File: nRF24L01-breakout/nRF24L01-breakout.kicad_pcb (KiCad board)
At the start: 2 copper layers, 28.6 x 16.4 mm, 17 parts, among them J1 Conn_01x04_Female, J2 Conn_01x04_Female, U1 NRF24L01, U2 Antenna_PCB_2.4GHz_50Ohm, U3 Balun_2450BM14A0002, Y1 Crystal_GND24_Small

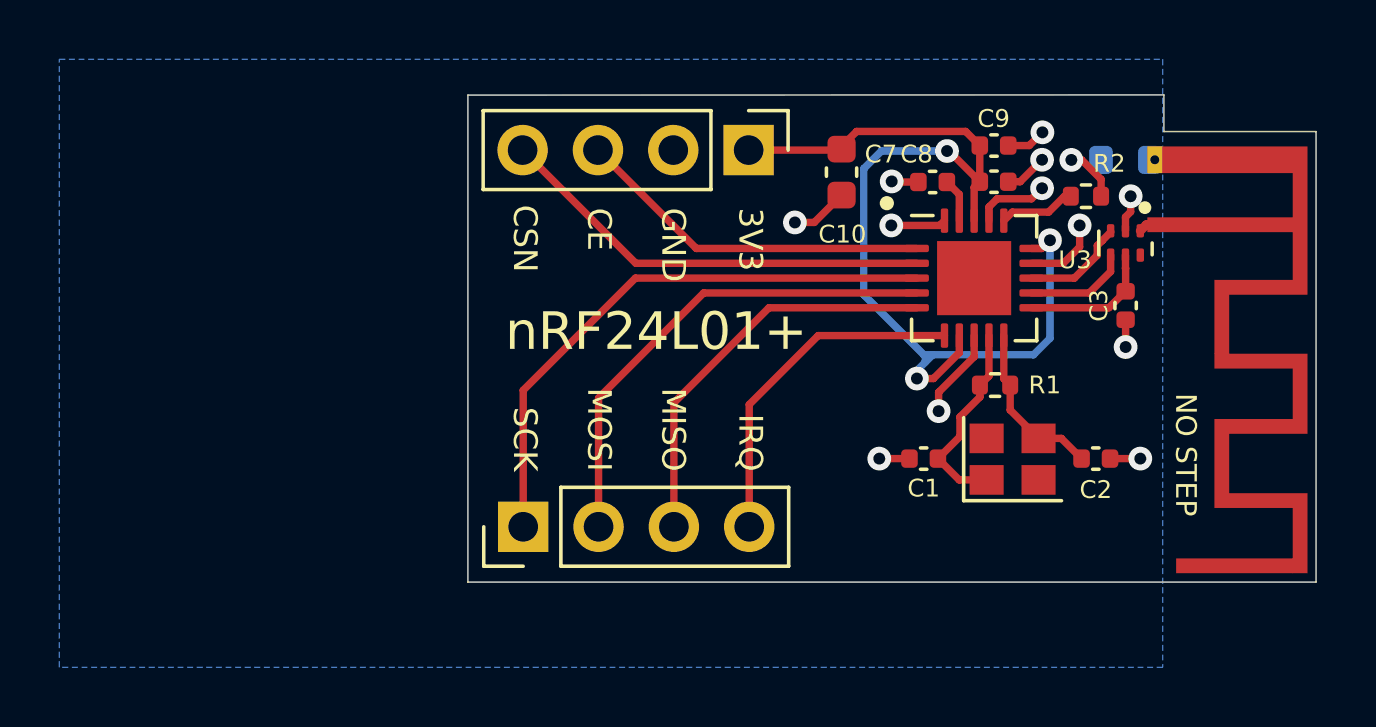
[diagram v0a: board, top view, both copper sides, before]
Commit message: Spread out signal traces
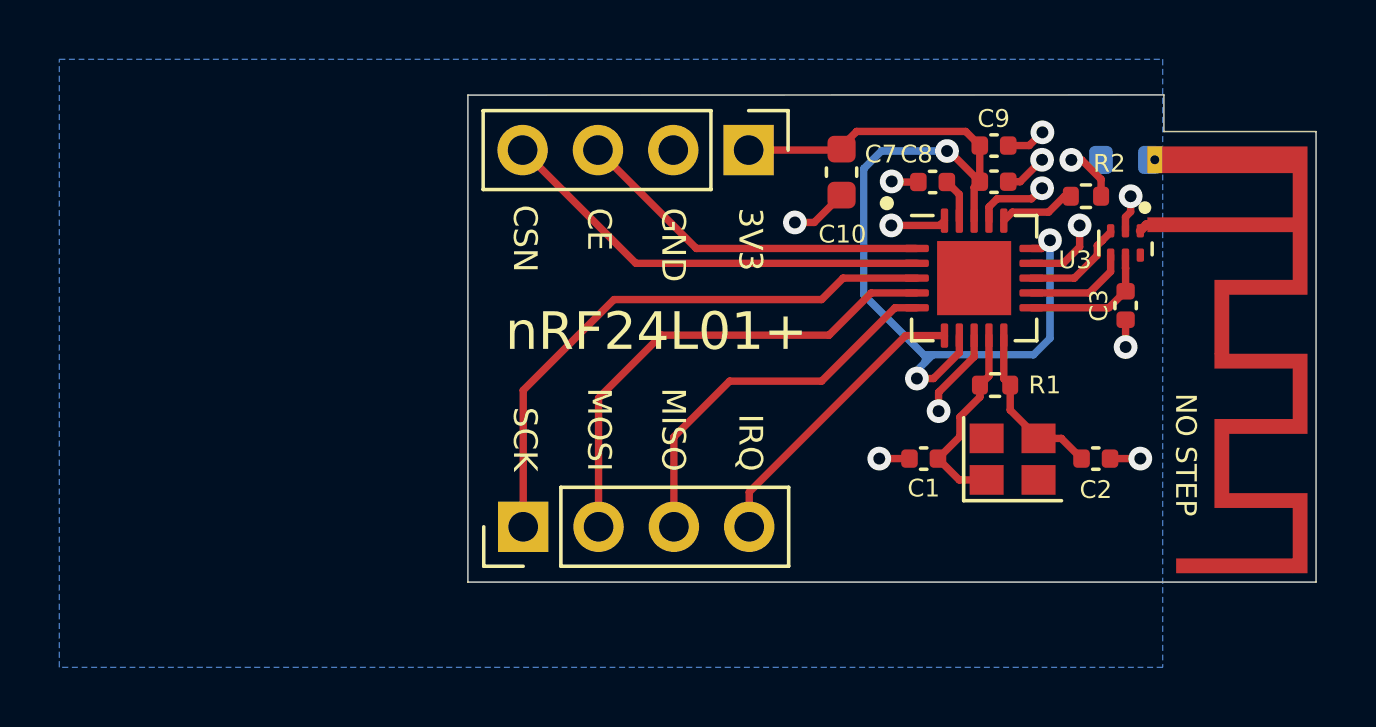
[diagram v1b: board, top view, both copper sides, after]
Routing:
- net IRQ: track 11.7 -> 9.94 mm
- net MISO: track 13.7 -> 13.0 mm
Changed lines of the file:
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@@
   (segment (start 167.0725 89.5418) (end 157.6038 89.5418) (width 0.25) (layer "F.Cu") (net 8))
   (segment (start 157.6038 89.5418) (end 153.787 85.725) (width 0.25) (layer "F.Cu") (net 8))
-  (segment (start 157.5902 90.0418) (end 153.807 93.825) (width 0.25) (layer "F.Cu") (net 9))
+  (segment (start 156.867 90.765) (end 153.807 93.825) (width 0.25) (layer "F.Cu") (net 9))
+  (segment (start 163.867 90.765) (end 156.867 90.765) (width 0.25) (layer "F.Cu") (net 9))
+  (segment (start 164.5902 90.0418) (end 163.867 90.765) (width 0.25) (layer "F.Cu") (net 9))
+  (segment (start 167.0725 90.0418) (end 164.5902 90.0418) (width 0.25) (layer "F.Cu") (net 9))
   (segment (start 153.807 93.825) (end 153.807 98.425) (width 0.25) (layer "F.Cu") (net 9))
-  (segment (start 167.0725 90.0418) (end 157.5902 90.0418) (width 0.25) (layer "F.Cu") (net 9))
-  (segment (start 167.0725 90.5418) (end 159.8902 90.5418) (width 0.25) (layer "F.Cu") (net 10))
+  (segment (start 167.0725 90.5418) (end 165.5402 90.5418) (width 0.25) (layer "F.Cu") (net 10))
+  (segment (start 165.5402 90.5418) (end 164.117 91.965) (width 0.25) (layer "F.Cu") (net 10))
+  (segment (start 164.117 91.965) (end 158.467 91.965) (width 0.25) (layer "F.Cu") (net 10))
+  (segment (start 158.467 91.965) (end 156.347 94.085) (width 0.25) (layer "F.Cu") (net 10))
   (segment (start 156.347 94.085) (end 156.347 98.425) (width 0.25) (layer "F.Cu") (net 10))
-  (segment (start 159.8902 90.5418) (end 156.347 94.085) (width 0.25) (layer "F.Cu") (net 10))
-  (segment (start 158.887 94.245) (end 158.887 98.425) (width 0.25) (layer "F.Cu") (net 11))
-  (segment (start 167.0725 91.0418) (end 162.0902 91.0418) (width 0.25) (layer "F.Cu") (net 11))
-  (segment (start 162.0902 91.0418) (end 158.887 94.245) (width 0.25) (layer "F.Cu") (net 11))
-  (segment (start 161.427 94.305) (end 161.427 98.425) (width 0.25) (layer "F.Cu") (net 12))
-  (segment (start 168.01 91.9793) (end 163.7527 91.9793) (width 0.25) (layer "F.Cu") (net 12))
-  (segment (start 163.7527 91.9793) (end 161.427 94.305) (width 0.25) (layer "F.Cu") (net 12))
+  (segment (start 167.0725 91.0418) (end 166.3402 91.0418) (width 0.25) (layer "F.Cu") (net 11))
+  (segment (start 166.3402 91.0418) (end 163.867 93.515) (width 0.25) (layer "F.Cu") (net 11))
+  (segment (start 158.887 95.395) (end 158.887 98.425) (width 0.25) (layer "F.Cu") (net 11))
+  (segment (start 160.767 93.515) (end 158.887 95.395) (width 0.25) (layer "F.Cu") (net 11))
+  (segment (start 163.867 93.515) (end 160.767 93.515) (width 0.25) (layer "F.Cu") (net 11))
+  (segment (start 161.427 97.255) (end 161.427 98.425) (width 0.25) (layer "F.Cu") (net 12))
+  (segment (start 168.01 91.9793) (end 166.7027 91.9793) (width 0.25) (layer "F.Cu") (net 12))
+  (segment (start 166.7027 91.9793) (end 161.427 97.255) (width 0.25) (layer "F.Cu") (net 12))
   (segment (start 174.995 88.2316) (end 175.005 88.2416) (width 0.25) (layer "F.Cu") (net 13))
   (segment (start 177.3 88.2416) (end 174.817 88.2416) (width 0.3048) (layer "F.Cu") (net 13))
